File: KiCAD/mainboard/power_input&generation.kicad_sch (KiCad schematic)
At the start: 0 parts

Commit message: yaaaa
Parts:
- added C24, C82, C96: 100 uF, tp_library:CAP_EEEFT1V101AP, symbol Device:C_Polarized_US
- added C71, C72, C73, C74: 10 V, Capacitor_SMD:C_0805_2012Metric_Pad1.18x1.45mm_HandSolder, symbol Device:C
- added D12: LED, LED_SMD:LED_0603_1608Metric_Pad1.05x0.95mm_HandSolder, symbol Device:LED
- added R117: R_US, symbol Device:R_US
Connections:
- new net: D12.2 (A), R117.1
- new net: C24.1, C71.1, C72.1, C73.1, C74.1, C82.1, C96.1, R117.2
- new net GND: C24.2, C71.2, C72.2, C73.2, C74.2, C82.2, C96.2, D12.1 (K)

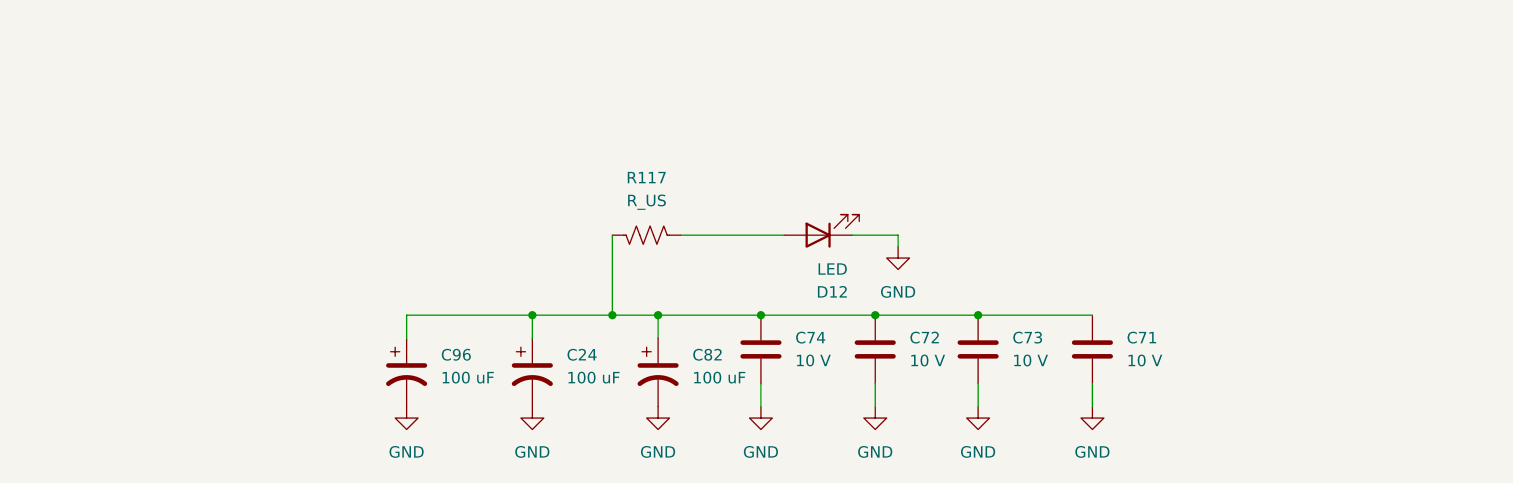
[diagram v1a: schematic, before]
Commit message: added footprints
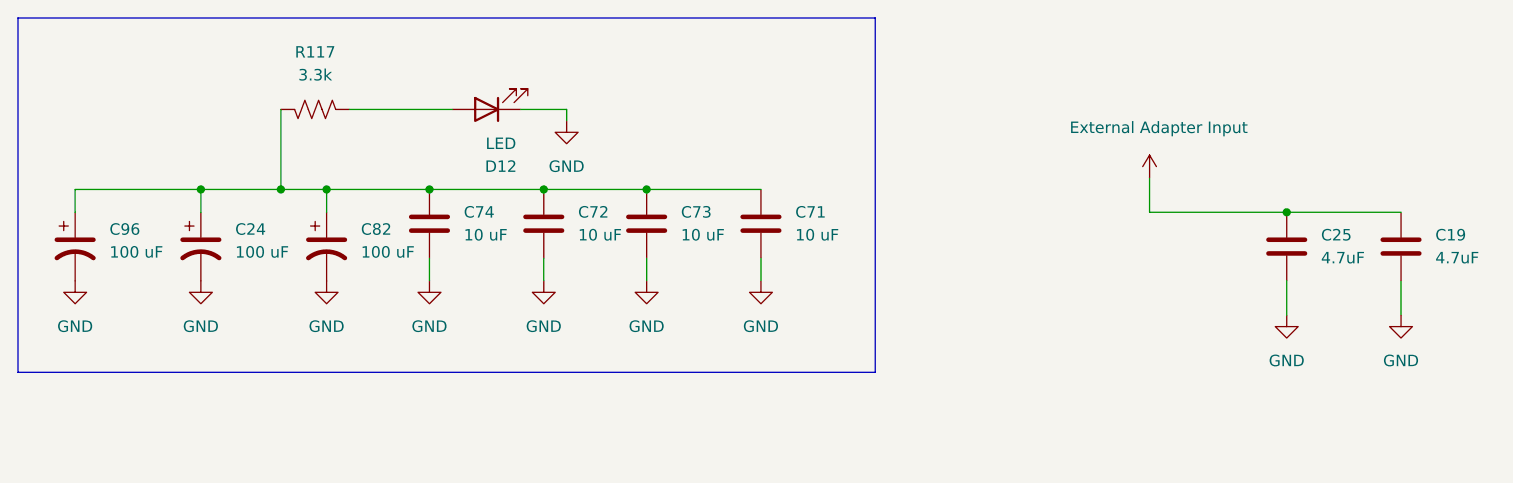
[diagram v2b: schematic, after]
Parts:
- added C19, C25: 4.7uF, Capacitor_SMD:C_0603_1608Metric_Pad1.08x0.95mm_HandSolder, symbol Device:C
- C71, C72, C73, C74: value 10 V -> 10 uF
- R117: value R_US -> 3.3k
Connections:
- net GND: now also C19.2, C25.2
- new net External Adapter Input: C19.1, C25.1
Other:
- moved on the sheet: C24, C71, C72, C73, C74, C82, C96, D12, R117

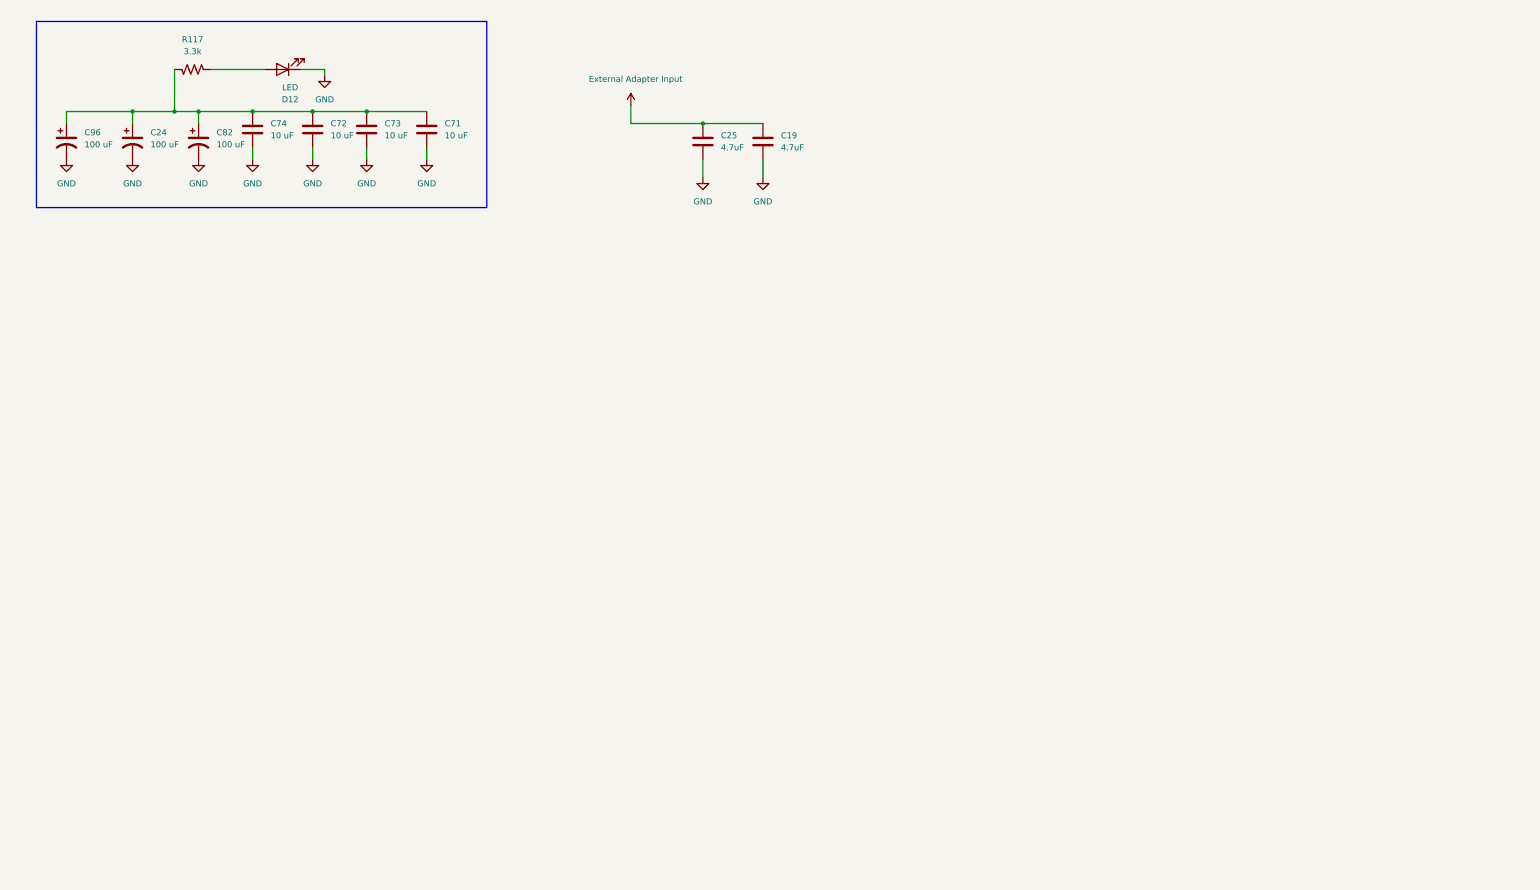
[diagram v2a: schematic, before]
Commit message: started power gen input schematic, need to source correct input for 5V buck converter, finished 5V to 3v3 buck converter, need to start the 1.2, 1.8, and buffer 3v3
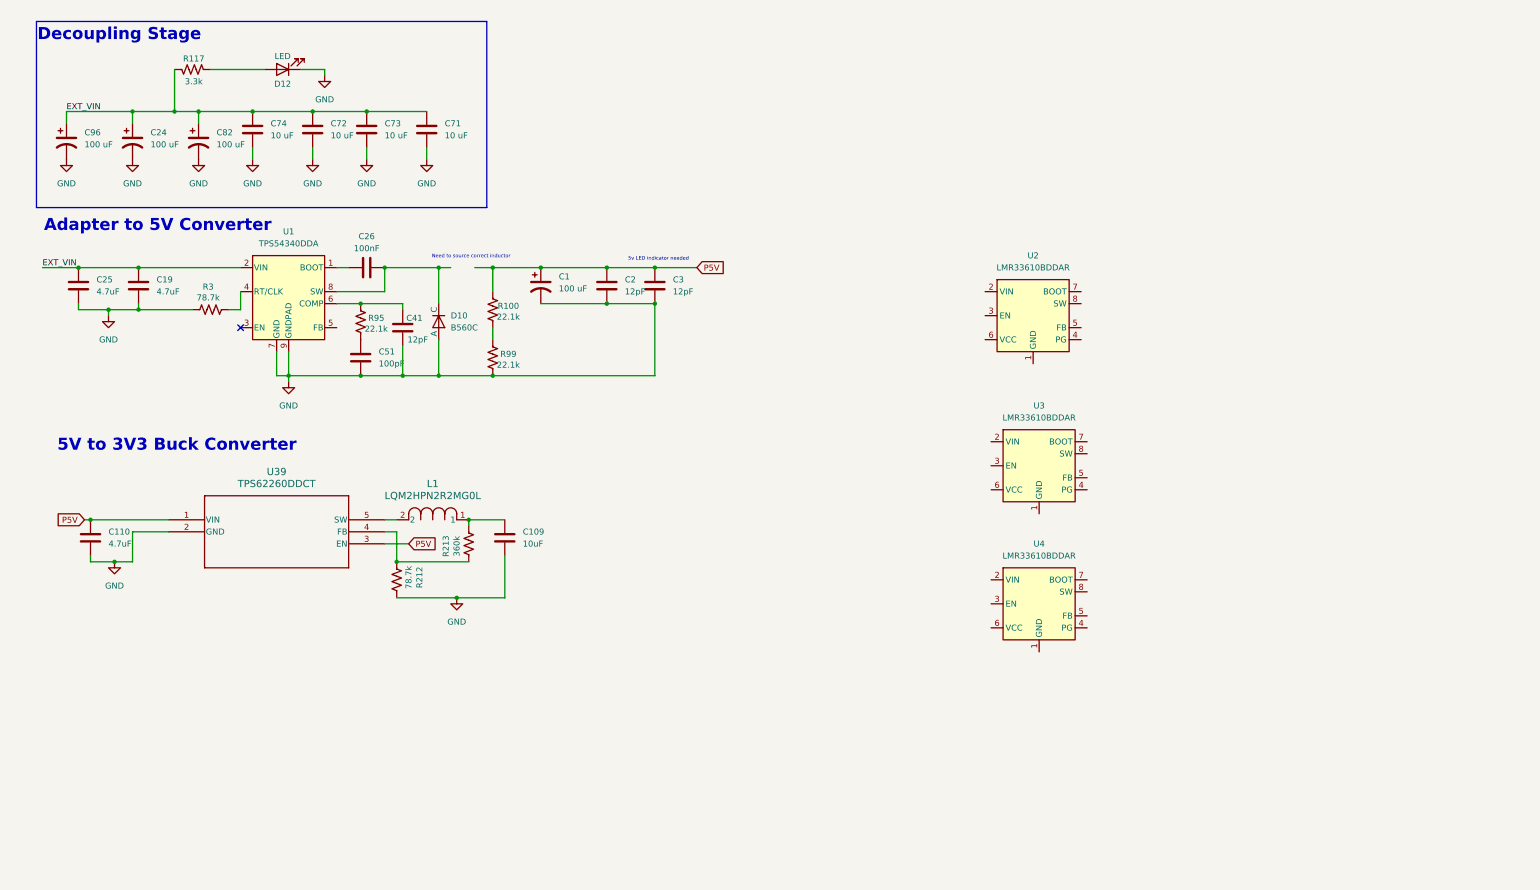
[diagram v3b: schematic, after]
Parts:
- added C1: 100 uF, tp_library:CAP_EEEFT1V101AP, symbol Device:C_Polarized_US
- added C109: 10uF, Capacitor_SMD:C_0603_1608Metric_Pad1.08x0.95mm_HandSolder, symbol Device:C
- added C110: 4.7uF, Capacitor_SMD:C_0603_1608Metric_Pad1.08x0.95mm_HandSolder, symbol Device:C
- added C2, C3, C41: 12pF, Capacitor_SMD:C_0603_1608Metric_Pad1.08x0.95mm_HandSolder, symbol Device:C
- added C26: 100nF, Capacitor_SMD:C_0603_1608Metric_Pad1.08x0.95mm_HandSolder, symbol Device:C
- added C51: 100pF, Capacitor_SMD:C_0603_1608Metric_Pad1.08x0.95mm_HandSolder, symbol Device:C
- added D10: B560C, tp_library:SMC_DIO, symbol ZMM22:Diode
- added L1: LQM2HPN2R2MG0L, tp_library:IND_LQM2HPN2R2MG0L_MUR, symbol tp_library:LQM2HPN2R2MG0L
- added R100, R95, R99: 22.1k, Resistor_SMD:R_0402_1005Metric, symbol Device:R_US
- added R212, R3: 78.7k, Resistor_SMD:R_0402_1005Metric, symbol Device:R_US
- added R213: 360k, Resistor_SMD:R_0402_1005Metric, symbol Device:R_US
- added U1: TPS54340DDA, Package_SO:TI_SO-PowerPAD-8_ThermalVias, symbol Regulator_Switching:TPS54340DDA
- added U2, U3, U4: LMR33610BDDAR, Package_SO:Texas_HSOP-8-1EP_3.9x4.9mm_P1.27mm_ThermalVias, symbol Regulator_Switching:LMR33610BDDAR
- added U39: TPS62260DDCT, tp_library:DDC5, symbol tp_library:TPS62260DDCT
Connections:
- net External Adapter Input is gone; now on net EXT_VIN: C19.1, C25.1
- net GND: now also C1.2, C109.2, C110.2, C2.2, C3.2, C41.2, C51.2, D10.1 (A), R212.1, R3.2, R99.2, U1.7 (GND), U1.9 (GNDPAD), U39.2 (GND)
- net EXT_VIN: now reaches C24.1, C71.1, C72.1, C73.1, C74.1, C82.1, C96.1, R117.2
- net EXT_VIN: now also U1.2 (VIN)
- new net: R212.2, R213.2, U39.4 (FB)
- new net: L1.2, U39.5 (SW)
- new net: C26.1, U1.1 (BOOT)
- new net: C26.2, D10.2 (C), U1.8 (SW)
- new net: U4.1 (GND), U4.9 (GND)
- new net: R100.2, R99.1
- new net: C41.1, R95.1, U1.6 (COMP)
- new net: C109.1, L1.1, R213.1
- new net: U2.1 (GND), U2.9 (GND)
- new net: R3.1, U1.4 (RT/CLK)
- new net: C51.1, R95.2
- new net: U3.1 (GND), U3.9 (GND)
- new net P5V: C1.1, C110.1, C2.1, C3.1, R100.1, U39.1 (VIN), U39.3 (EN)
- no-connect marks 0 -> 1
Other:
- note added: "5V to 3V3 Buck Converter"
- note added: "5v LED indicator needed"
- note added: "Adapter to 5V Converter"
- note added: "Decoupling Stage"
- note added: "Need to source correct inductor"
- moved on the sheet: C19, C25

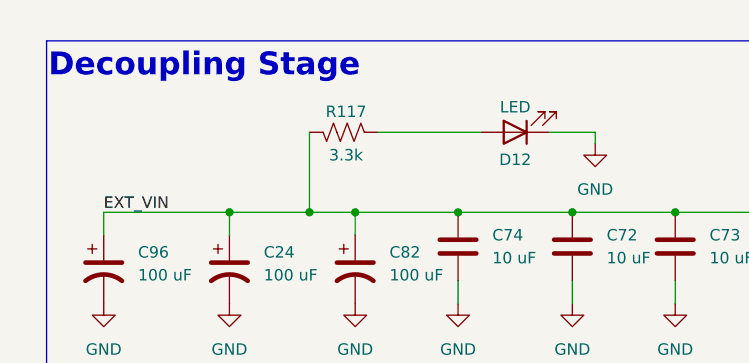
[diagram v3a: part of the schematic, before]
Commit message: replaced with 0805 all passives in DLPC
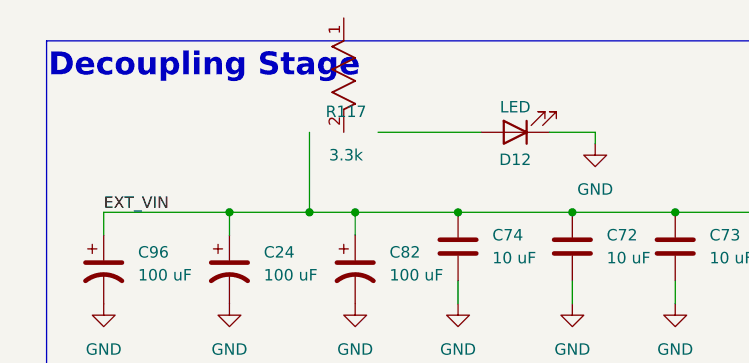
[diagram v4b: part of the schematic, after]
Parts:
- R117: footprint (none) -> RES_ERJP06_PAN; symbol Device:R_US -> ERJP06F3301V:ERJP06F3301V
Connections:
- net EXT_VIN: no longer R117.2
- net at R117.1: no longer D12.2 (A)
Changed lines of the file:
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@@
 	)
 	(symbol
-		(lib_id "Device:R_US")
+		(lib_id "ERJP06F3301V:ERJP06F3301V")
 		(at 46.99 26.67 270)
 		(mirror x)
@@
 			)
 		)
-		(property "Footprint" ""
-			(at 46.736 25.654 90)
+		(property "Footprint" "RES_ERJP06_PAN"
+			(at 46.99 26.67 0)
 			(effects
 				(font
 					(size 1.27 1.27)
+					(italic yes)
 				)
 				(hide yes)
 			)
 		)
-		(property "Datasheet" "~"
+		(property "Datasheet" "ERJP06F3301V"
 			(at 46.99 26.67 0)
 			(effects
 				(font
 					(size 1.27 1.27)
+					(italic yes)
 				)
 				(hide yes)

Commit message: changes to all schematic files fixing ERC errors
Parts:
- removed U2, U3, U4: LMR33610BDDAR, Package_SO:Texas_HSOP-8-1EP_3.9x4.9mm_P1.27mm_ThermalVias, symbol Regulator_Switching:LMR33610BDDAR
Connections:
- net EXT_VIN: now also R117.2
- net at R117.1: now also D12.2 (A)
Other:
- moved on the sheet: D12, R117

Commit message: more ERC knocked out
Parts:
- renumbered L1 to L12, U1 to U26
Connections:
- no-connect marks 1 -> 2
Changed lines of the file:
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@@
 	)
 	(junction
+		(at 53.34 68.58)
+		(diameter 0)
+		(color 0 0 0 0)
+	)
+	(junction
+		(at 40.64 121.92)
+		(diameter 0)
+		(color 0 0 0 0)
+	)
+	(junction
 		(at 105.41 121.92)
 		(diameter 0)
@@
 	)
 	(no_connect
+		(at 77.47 81.28)
+	)
+	(no_connect
 		(at 57.15 81.28)
 	)
@@
 	(wire
 		(pts
-			(xy 25.4 121.92) (xy 41.91 121.92)
+			(xy 25.4 121.92) (xy 40.64 121.92)
 		)
 		(stroke
@@
 	(wire
 		(pts
-			(xy 57.15 68.58) (xy 35.56 68.58)
+			(xy 57.15 68.58) (xy 53.34 68.58)
 		)
 		(stroke
@@
 	(wire
 		(pts
+			(xy 40.64 121.92) (xy 41.91 121.92)
+		)
+		(stroke
+			(width 0)
+			(type default)
+		)
+	)
+	(wire
+		(pts
 			(xy 87.63 121.92) (xy 90.17 121.92)
 		)
@@
 	(wire
 		(pts
+			(xy 53.34 68.58) (xy 35.56 68.58)
+		)
+		(stroke
+			(width 0)
+			(type default)
+		)
+	)
+	(wire
+		(pts
 			(xy 120.65 68.58) (xy 134.62 68.58)
 		)
@@
 	)
 	(symbol
+		(lib_id "power:PWR_FLAG")
+		(at 53.34 68.58 0)
+		(unit 1)
+		(exclude_from_sim no)
+		(in_bom yes)
+		(on_board yes)
+		(dnp no)
+		(property "Reference" "#FLG06"
+			(at 53.34 66.675 0)
+			(effects
+				(font
+					(size 1.27 1.27)
+				)
+				(hide yes)
+			)
+		)
+		(property "Value" "PWR_FLAG"
+			(at 54.102 63.754 0)
+			(effects
+				(font
+					(size 1.27 1.27)
+				)
+			)
+		)
+		(property "Footprint" ""
+			(at 53.34 68.58 0)
+			(effects
+				(font
+					(size 1.27 1.27)
+				)
+				(hide yes)
+			)
+		)
+		(property "Datasheet" "~"
+			(at 53.34 68.58 0)
+			(effects
+				(font
+					(size 1.27 1.27)
+				)
+				(hide yes)
+			)
+		)
+		(property "Description" "Special symbol for telling ERC where power comes from"
+			(at 53.34 68.58 0)
+			(effects
+				(font
+					(size 1.27 1.27)
+				)
+				(hide yes)
+			)
+		)
+		(pin "1"
+		)
+		(instances
+			(project "mainboard"
+				(path "/38e83f42-2cf9-4799-a46f-ca415d95b90a/1598073b-cadd-4ddc-981f-6a3774f37a0f"
+					(reference "#FLG06")
+					(unit 1)
+				)
+			)
+		)
+	)
+	(symbol
 		(lib_id "power:GND")
 		(at 85.09 27.94 0)
@@
 	)
 	(symbol
+		(lib_id "power:PWR_FLAG")
+		(at 40.64 121.92 0)
+		(unit 1)
+		(exclude_from_sim no)
+		(in_bom yes)
+		(on_board yes)
+		(dnp no)
+		(property "Reference" "#FLG07"
+			(at 40.64 120.015 0)
+			(effects
+				(font
+					(size 1.27 1.27)
+				)
+				(hide yes)
+			)
+		)
+		(property "Value" "PWR_FLAG"
+			(at 41.402 117.094 0)
+			(effects
+				(font
+					(size 1.27 1.27)
+				)
+			)
+		)
+		(property "Footprint" ""
+			(at 40.64 121.92 0)
+			(effects
+				(font
+					(size 1.27 1.27)
+				)
+				(hide yes)
+			)
+		)
+		(property "Datasheet" "~"
+			(at 40.64 121.92 0)
+			(effects
+				(font
+					(size 1.27 1.27)
+				)
+				(hide yes)
+			)
+		)
+		(property "Description" "Special symbol for telling ERC where power comes from"
+			(at 40.64 121.92 0)
+			(effects
+				(font
+					(size 1.27 1.27)
+				)
+				(hide yes)
+			)
+		)
+		(pin "1"
+		)
+		(instances
+			(project "mainboard"
+				(path "/38e83f42-2cf9-4799-a46f-ca415d95b90a/1598073b-cadd-4ddc-981f-6a3774f37a0f"
+					(reference "#FLG07")
+					(unit 1)
+				)
+			)
+		)
+	)
+	(symbol
 		(lib_id "Device:C")
 		(at 91.44 81.28 0)
@@
 		(dnp no)
 		(fields_autoplaced yes)
-		(property "Reference" "L1"
+		(property "Reference" "L12"
 			(at 97.79 114.3 0)
 			(effects
@@
 			(project ""
 				(path "/38e83f42-2cf9-4799-a46f-ca415d95b90a/1598073b-cadd-4ddc-981f-6a3774f37a0f"
-					(reference "L1")
+					(reference "L12")
 					(unit 1)
 				)
@@
 		(dnp no)
 		(fields_autoplaced yes)
-		(property "Reference" "U1"
+		(property "Reference" "U26"
 			(at 67.31 60.96 0)
 			(effects
@@
 			(project ""
 				(path "/38e83f42-2cf9-4799-a46f-ca415d95b90a/1598073b-cadd-4ddc-981f-6a3774f37a0f"
-					(reference "U1")
+					(reference "U26")
 					(unit 1)
 				)

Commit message: getting started on power generation
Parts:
- added D13: D_Zener, symbol Device:D_Zener
- added Q1: PMOS, symbol Simulation_SPICE:PMOS
- added R1, R127: 100k, RES_RMCF0805_STP, symbol RMCF0805FG100K:RMCF0805FG100K
- added R137: 20k, Resistor_SMD:R_0402_1005Metric, symbol Device:R_US
- added R138: 15k, Resistor_SMD:R_0402_1005Metric, symbol Device:R_US
- renumbered C24 to C83
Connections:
- net EXT_VIN: no longer C71.1, C72.1, C73.1, C74.1, C82.1, C83.1, C96.1, R117.2
- net VIN_LED: now reaches D12.2 (A), R117.1
- new net: D13.1 (K), Q1.3 (S), R127.2, R138.1
- new net: R137.2, R138.2
- new net EXT_VIN_SW_G: D13.2 (A), Q1.2 (G), R127.1, R137.1
- new net VIN: C71.1, C72.1, C73.1, C74.1, C82.1, C83.1, C96.1, Q1.1 (D), R117.2
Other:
- moved on the sheet: C1, C109, C110, C19, C2, C25, C26, C3, C41, C51, C71, C72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

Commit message: work
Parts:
- removed R1: 100k, RES_RMCF0805_STP, symbol RMCF0805FG100K:RMCF0805FG100K
- added C10, C11, C18, C23, C24, C28, C8, C9: 22uF, Capacitor_SMD:C_0603_1608Metric_Pad1.08x0.95mm_HandSolder, symbol Device:C
- added C12, C32: 100nF, Capacitor_SMD:C_0603_1608Metric_Pad1.08x0.95mm_HandSolder, symbol Device:C
- added C16, C43: 4.7uF, Capacitor_SMD:C_0603_1608Metric_Pad1.08x0.95mm_HandSolder, symbol Device:C
- added C17, C44: 220nF, Capacitor_SMD:C_0603_1608Metric_Pad1.08x0.95mm_HandSolder, symbol Device:C
- added U1: XAL5030-472MEC, tp_library:XAL5030-472MEC_COC, symbol tp_library:XAL5030-472MEC
- added U2, U3: LMR33610BDDAR, Package_SO:Texas_HSOP-8-1EP_3.9x4.9mm_P1.27mm_ThermalVias, symbol Regulator_Switching:LMR33610BDDAR
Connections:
- net EXT_VIN: now also C71.1, C72.1, C73.1, C74.1, C82.1, C83.1, C96.1, D13.1 (K), Q1.3 (S), R117.2, R127.2, R138.1; no longer C19.1, C25.1, U26.2 (VIN)
- net GND: now also C16.2, C17.2, C43.2, C44.2, U2.1 (GND), U2.9 (GND), U3.1 (GND), U3.9 (GND)
- net P5V: now also U1.2
- net at C26.2, D10.2 (C), U26.8 (SW): now also U1.1
- net P3V3V: now reaches C109.1, L12.1, R213.1
- removed net VIN: C71.1, C72.1, C73.1, C74.1, C82.1, C83.1, C96.1, Q1.1 (D), R117.2
- new net: C43.1, C44.1, U2.2 (VIN)
- new net: C18.1, C23.1, C24.1, C28.1, C32.1
- new net: C18.2, C23.2, C24.2, C28.2, C32.2
- new net: C10.1, C11.1, C12.1, C8.1, C9.1
- new net: C10.2, C11.2, C12.2, C8.2, C9.2
- new net: C16.1, C17.1, U3.2 (VIN)
- new net: C19.1, C25.1, U26.2 (VIN)
- new net FPGA_PWREN: U2.3 (EN), U3.3 (EN)
- new net P1P2V_BOOT: U2.7 (BOOT), U3.7 (BOOT)
- new net P1P2V_SW: U2.8 (SW), U3.8 (SW)
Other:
- note added: "3V3 To 1.2V Converter"
- note added: "3V3 To 1.8V Converter"
- note added: "Input Decoupling Stage"
- note removed: "Decoupling Stage"
- note removed: "Need to source correct inductor"
- moved on the sheet: C1, C109, C110, C19, C2, C25, C26, C3, C41, C51, C71, C72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
